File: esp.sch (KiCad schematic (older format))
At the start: 13 parts, among them P1 V_SEL, P2 FTDI, P3 ESP-01, P4 TX_SEL, SW1 RST, SW2 GIPO0

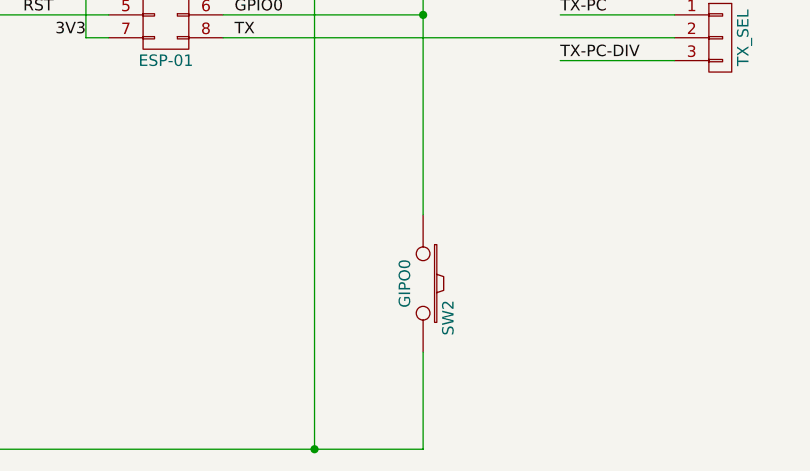
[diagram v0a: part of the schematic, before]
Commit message: corrected typo on legend
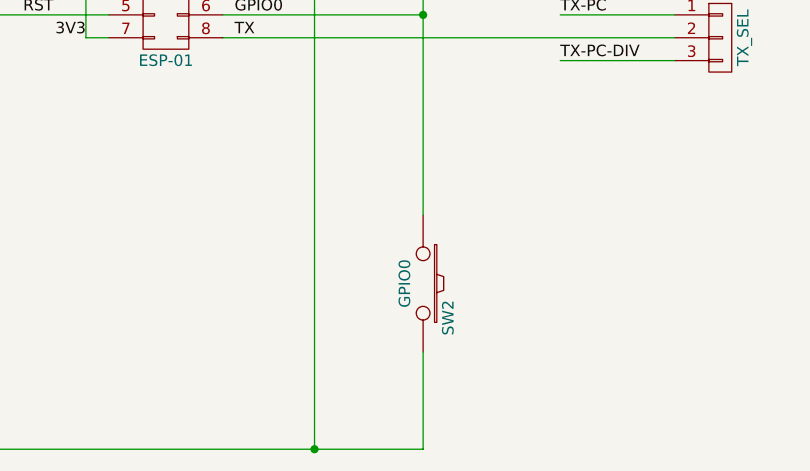
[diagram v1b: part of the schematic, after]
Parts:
- SW2: value GIPO0 -> GPIO0
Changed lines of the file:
@@
 P 6350 5525
 F 0 "SW2" H 6500 5635 50  0000 C CNN
-F 1 "GIPO0" H 6350 5445 50  0000 C CNN
+F 1 "GPIO0" H 6350 5445 50  0000 C CNN
 F 2 "esp:SW_PUSH_SMALL" H 6350 5525 60  0001 C CNN
 F 3 "" H 6350 5525 60  0000 C CNN
